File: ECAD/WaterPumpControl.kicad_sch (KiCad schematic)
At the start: 2 parts, among them Q7 NCE3018AS, Q8 NCE3018AS

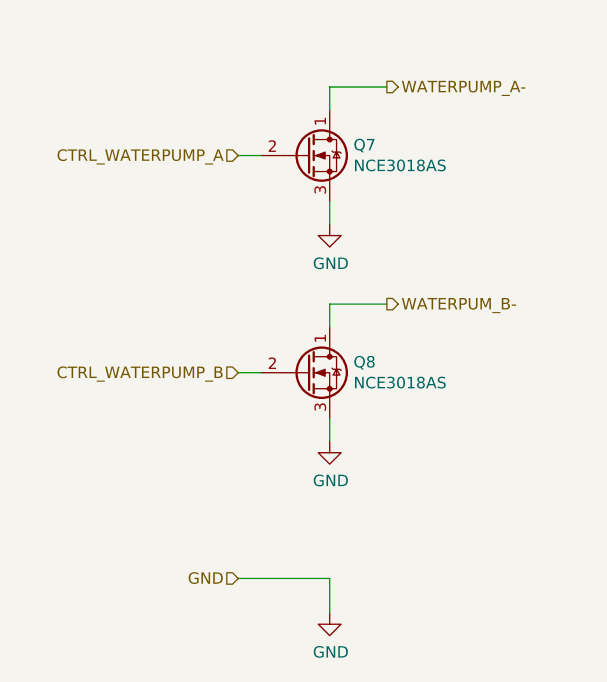
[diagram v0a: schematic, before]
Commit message: pcb layout has started, still ned to make 5V to 3.3V power supply, add dip switch do individually control input power of each switch, 5V or 12V
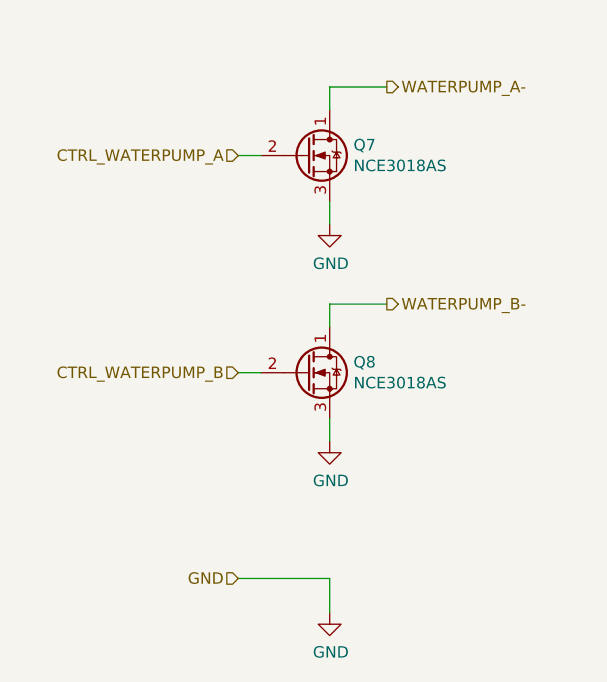
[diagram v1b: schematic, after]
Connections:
- net WATERPUM_B- renamed WATERPUMP_B-
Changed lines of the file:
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@@
     (effects (font (size 1.27 1.27)) (justify left))
   )
-  (hierarchical_label "WATERPUM_B-" (shape output) (at 158.75 100.33 0)
+  (hierarchical_label "WATERPUMP_B-" (shape output) (at 158.75 100.33 0)
     (effects (font (size 1.27 1.27)) (justify left))
   )

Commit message: finishing up pcb, only billonly bill of materials need to be done to be compatible with lc from jlcpcb
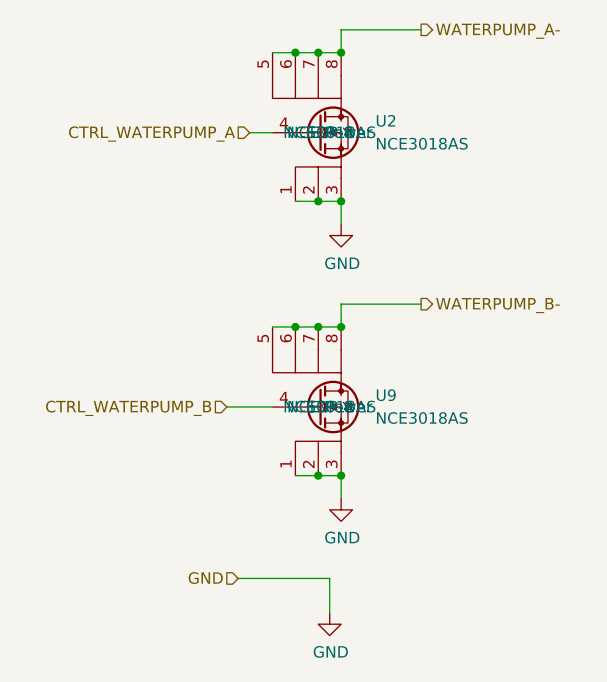
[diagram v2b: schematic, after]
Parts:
- removed Q7, Q8: NCE3018AS, Package_SO:SOP-8_3.9x4.9mm_P1.27mm, symbol Device:Q_NMOS_DGS
- added U2, U9: NCE3018AS, Package_SO:SO-8_3.9x4.9mm_P1.27mm, symbol Transistors:NCE3018AS
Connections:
- net CTRL_WATERPUMP_A: now also U2.4
- net CTRL_WATERPUMP_B: now also U9.4
- net GND: now also U2.1, U2.2, U2.3, U9.1, U9.2, U9.3
- net WATERPUMP_A-: now also U2.5, U2.6, U2.7, U2.8
- net WATERPUMP_B-: now also U9.5, U9.6, U9.7, U9.8
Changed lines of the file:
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@@
 (kicad_sch (version 20210126) (generator eeschema)
   (paper "A4")
-  (wire (pts (xy 142.24 83.82) (xy 144.78 83.82))
-    (stroke (width 0) (type solid) (color 0 0 0 0))
-  )
-  (wire (pts (xy 142.24 107.95) (xy 144.78 107.95))
+  (junction (at 148.59 72.39) (diameter 0.9144) (color 0 0 0 0))
+  (junction (at 148.59 102.87) (diameter 0.9144) (color 0 0 0 0))
+  (junction (at 151.13 72.39) (diameter 0.9144) (color 0 0 0 0))
+  (junction (at 151.13 88.9) (diameter 0.9144) (color 0 0 0 0))
+  (junction (at 151.13 102.87) (diameter 0.9144) (color 0 0 0 0))
+  (junction (at 151.13 119.38) (diameter 0.9144) (color 0 0 0 0))
+  (junction (at 153.67 72.39) (diameter 0.9144) (color 0 0 0 0))
+  (junction (at 153.67 88.9) (diameter 0.9144) (color 0 0 0 0))
+  (junction (at 153.67 102.87) (diameter 0.9144) (color 0 0 0 0))
+  (junction (at 153.67 119.38) (diameter 0.9144) (color 0 0 0 0))
+  (wire (pts (xy 140.97 111.76) (xy 146.05 111.76))
     (stroke (width 0) (type solid) (color 0 0 0 0))
   )
@@
     (stroke (width 0) (type solid) (color 0 0 0 0))
   )
-  (wire (pts (xy 152.4 76.2) (xy 158.75 76.2))
+  (wire (pts (xy 143.51 81.28) (xy 146.05 81.28))
     (stroke (width 0) (type solid) (color 0 0 0 0))
   )
-  (wire (pts (xy 152.4 78.74) (xy 152.4 76.2))
+  (wire (pts (xy 146.05 72.39) (xy 148.59 72.39))
     (stroke (width 0) (type solid) (color 0 0 0 0))
   )
-  (wire (pts (xy 152.4 88.9) (xy 152.4 91.44))
+  (wire (pts (xy 146.05 102.87) (xy 148.59 102.87))
     (stroke (width 0) (type solid) (color 0 0 0 0))
   )
-  (wire (pts (xy 152.4 100.33) (xy 158.75 100.33))
+  (wire (pts (xy 148.59 72.39) (xy 151.13 72.39))
     (stroke (width 0) (type solid) (color 0 0 0 0))
   )
-  (wire (pts (xy 152.4 102.87) (xy 152.4 100.33))
+  (wire (pts (xy 148.59 88.9) (xy 151.13 88.9))
     (stroke (width 0) (type solid) (color 0 0 0 0))
   )
-  (wire (pts (xy 152.4 113.03) (xy 152.4 115.57))
+  (wire (pts (xy 148.59 102.87) (xy 151.13 102.87))
+    (stroke (width 0) (type solid) (color 0 0 0 0))
+  )
+  (wire (pts (xy 148.59 119.38) (xy 151.13 119.38))
+    (stroke (width 0) (type solid) (color 0 0 0 0))
+  )
+  (wire (pts (xy 151.13 72.39) (xy 153.67 72.39))
+    (stroke (width 0) (type solid) (color 0 0 0 0))
+  )
+  (wire (pts (xy 151.13 88.9) (xy 153.67 88.9))
+    (stroke (width 0) (type solid) (color 0 0 0 0))
+  )
+  (wire (pts (xy 151.13 102.87) (xy 153.67 102.87))
+    (stroke (width 0) (type solid) (color 0 0 0 0))
+  )
+  (wire (pts (xy 151.13 119.38) (xy 153.67 119.38))
     (stroke (width 0) (type solid) (color 0 0 0 0))
   )
@@
     (stroke (width 0) (type solid) (color 0 0 0 0))
   )
-  (hierarchical_label "CTRL_WATERPUMP_A" (shape input) (at 142.24 83.82 180)
-    (effects (font (size 1.27 1.27)) (justify right))
+  (wire (pts (xy 153.67 69.85) (xy 162.56 69.85))
+    (stroke (width 0) (type solid) (color 0 0 0 0))
   )
-  (hierarchical_label "CTRL_WATERPUMP_B" (shape input) (at 142.24 107.95 180)
+  (wire (pts (xy 153.67 72.39) (xy 153.67 69.85))
+    (stroke (width 0) (type solid) (color 0 0 0 0))
+  )
+  (wire (pts (xy 153.67 88.9) (xy 153.67 91.44))
+    (stroke (width 0) (type solid) (color 0 0 0 0))
+  )
+  (wire (pts (xy 153.67 100.33) (xy 162.56 100.33))
+    (stroke (width 0) (type solid) (color 0 0 0 0))
+  )
+  (wire (pts (xy 153.67 102.87) (xy 153.67 100.33))
+    (stroke (width 0) (type solid) (color 0 0 0 0))
+  )
+  (wire (pts (xy 153.67 119.38) (xy 153.67 121.92))
+    (stroke (width 0) (type solid) (color 0 0 0 0))
+  )
+  (hierarchical_label "CTRL_WATERPUMP_B" (shape input) (at 140.97 111.76 180)
     (effects (font (size 1.27 1.27)) (justify right))
   )
@@
     (effects (font (size 1.27 1.27)) (justify right))
   )
-  (hierarchical_label "WATERPUMP_A-" (shape output) (at 158.75 76.2 0)
+  (hierarchical_label "CTRL_WATERPUMP_A" (shape input) (at 143.51 81.28 180)
+    (effects (font (size 1.27 1.27)) (justify right))
+  )
+  (hierarchical_label "WATERPUMP_A-" (shape output) (at 162.56 69.85 0)
     (effects (font (size 1.27 1.27)) (justify left))
   )
-  (hierarchical_label "WATERPUMP_B-" (shape output) (at 158.75 100.33 0)
+  (hierarchical_label "WATERPUMP_B-" (shape output) (at 162.56 100.33 0)
     (effects (font (size 1.27 1.27)) (justify left))
-  )
-  (symbol (lib_id "power:GND") (at 152.4 91.44 0) (unit 1)
-    (in_bom yes) (on_board yes)
-    (property "Reference" "#PWR0136" (id 0) (at 152.4 97.79 0)
-      (effects (font (size 1.27 1.27)) hide)
-    )
-    (property "Value" "GND" (id 1) (at 152.527 95.8342 0))
-    (property "Footprint" "" (id 2) (at 152.4 91.44 0)
-      (effects (font (size 1.27 1.27)) hide)
-    )
-    (property "Datasheet" "" (id 3) (at 152.4 91.44 0)
-      (effects (font (size 1.27 1.27)) hide)
-    )
-    (pin "1")
-  )
-  (symbol (lib_id "power:GND") (at 152.4 115.57 0) (unit 1)
-    (in_bom yes) (on_board yes)
-    (property "Reference" "#PWR0137" (id 0) (at 152.4 121.92 0)
-      (effects (font (size 1.27 1.27)) hide)
-    )
-    (property "Value" "GND" (id 1) (at 152.527 119.9642 0))
-    (property "Footprint" "" (id 2) (at 152.4 115.57 0)
-      (effects (font (size 1.27 1.27)) hide)
-    )
-    (property "Datasheet" "" (id 3) (at 152.4 115.57 0)
-      (effects (font (size 1.27 1.27)) hide)
-    )
-    (pin "1")
   )
   (symbol (lib_id "power:GND") (at 152.4 134.62 0) (unit 1)
@@
     (pin "1")
   )
-  (symbol (lib_id "Device:Q_NMOS_DGS") (at 149.86 83.82 0) (unit 1)
+  (symbol (lib_id "power:GND") (at 153.67 91.44 0) (unit 1)
     (in_bom yes) (on_board yes)
-    (property "Reference" "Q7" (id 0) (at 155.0416 82.6516 0)
-      (effects (font (size 1.27 1.27)) (justify left))
-    )
-    (property "Value" "NCE3018AS" (id 1) (at 155.0416 84.963 0)
-      (effects (font (size 1.27 1.27)) (justify left))
-    )
-    (property "Footprint" "Package_SO:SOP-8_3.9x4.9mm_P1.27mm" (id 2) (at 154.94 81.28 0)
+    (property "Reference" "#PWR0136" (id 0) (at 153.67 97.79 0)
       (effects (font (size 1.27 1.27)) hide)
     )
-    (property "Datasheet" "~" (id 3) (at 149.86 83.82 0)
+    (property "Value" "GND" (id 1) (at 153.797 95.8342 0))
+    (property "Footprint" "" (id 2) (at 153.67 91.44 0)
+      (effects (font (size 1.27 1.27)) hide)
+    )
+    (property "Datasheet" "" (id 3) (at 153.67 91.44 0)
       (effects (font (size 1.27 1.27)) hide)
     )
     (pin "1")
-    (pin "2")
-    (pin "3")
   )
-  (symbol (lib_id "Device:Q_NMOS_DGS") (at 149.86 107.95 0) (unit 1)
+  (symbol (lib_id "power:GND") (at 153.67 121.92 0) (unit 1)
     (in_bom yes) (on_board yes)
-    (property "Reference" "Q8" (id 0) (at 155.0416 106.7816 0)
-      (effects (font (size 1.27 1.27)) (justify left))
-    )
-    (property "Value" "NCE3018AS" (id 1) (at 155.0416 109.093 0)
-      (effects (font (size 1.27 1.27)) (justify left))
-    )
-    (property "Footprint" "Package_SO:SOP-8_3.9x4.9mm_P1.27mm" (id 2) (at 154.94 105.41 0)
+    (property "Reference" "#PWR0101" (id 0) (at 153.67 128.27 0)
       (effects (font (size 1.27 1.27)) hide)
     )
-    (property "Datasheet" "~" (id 3) (at 149.86 107.95 0)
+    (property "Value" "GND" (id 1) (at 153.797 126.3142 0))
+    (property "Footprint" "" (id 2) (at 153.67 121.92 0)
+      (effects (font (size 1.27 1.27)) hide)
+    )
+    (property "Datasheet" "" (id 3) (at 153.67 121.92 0)
       (effects (font (size 1.27 1.27)) hide)
     )
     (pin "1")
+  )
+  (symbol (lib_name "Transistors:NCE3018AS_1") (lib_id "Transistors:NCE3018AS") (at 152.4 81.28 0) (unit 1)
+    (in_bom yes) (on_board yes)
+    (property "Reference" "U2" (id 0) (at 157.48 80.01 0)
+      (effects (font (size 1.27 1.27)) (justify left))
+    )
+    (property "Value" "NCE3018AS" (id 1) (at 157.48 82.55 0)
+      (effects (font (size 1.27 1.27)) (justify left))
+    )
+    (property "Footprint" "Package_SO:SO-8_3.9x4.9mm_P1.27mm" (id 2) (at 153.67 67.31 0)
+      (effects (font (size 1.27 1.27)) hide)
+    )
+    (property "Datasheet" "https://datasheetspdf.com/pdf-file/1273153/NCEPowerSemiconductor/NCE3018AS/1" (id 3) (at 153.67 67.31 0)
+      (effects (font (size 1.27 1.27)) hide)
+    )
+    (property "Manufacturer Number" "NCE3018AS" (id 4) (at 152.4 81.28 0))
+    (property "Package" "SOP-8" (id 5) (at 152.4 81.28 0))
+    (property "Manufacturer" "NCE Power" (id 6) (at 152.4 81.28 0))
+    (pin "5")
+    (pin "4")
+    (pin "1")
     (pin "2")
     (pin "3")
+    (pin "6")
+    (pin "7")
+    (pin "8")
+  )
+  (symbol (lib_id "Transistors:NCE3018AS") (at 152.4 111.76 0) (unit 1)
+    (in_bom yes) (on_board yes)
+    (property "Reference" "U9" (id 0) (at 157.48 110.49 0)
+      (effects (font (size 1.27 1.27)) (justify left))
+    )
+    (property "Value" "NCE3018AS" (id 1) (at 157.48 113.03 0)
+      (effects (font (size 1.27 1.27)) (justify left))
+    )
+    (property "Footprint" "Package_SO:SO-8_3.9x4.9mm_P1.27mm" (id 2) (at 153.67 97.79 0)
+      (effects (font (size 1.27 1.27)) hide)
+    )
+    (property "Datasheet" "https://datasheetspdf.com/pdf-file/1273153/NCEPowerSemiconductor/NCE3018AS/1" (id 3) (at 153.67 97.79 0)
+      (effects (font (size 1.27 1.27)) hide)
+    )
+    (property "Manufacturer Number" "NCE3018AS" (id 4) (at 152.4 111.76 0))
+    (property "Package" "SOP-8" (id 5) (at 152.4 111.76 0))
+    (property "Manufacturer" "NCE Power" (id 6) (at 152.4 111.76 0))
+    (pin "5")
+    (pin "4")
+    (pin "1")
+    (pin "2")
+    (pin "3")
+    (pin "6")
+    (pin "7")
+    (pin "8")
   )
 )

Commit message: adding production and step files
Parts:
- U2, U9: Package SOP-8 -> SOP-8_150mil
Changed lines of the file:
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@@
     )
     (property "Manufacturer Number" "NCE3018AS" (id 4) (at 152.4 81.28 0))
-    (property "Package" "SOP-8" (id 5) (at 152.4 81.28 0))
+    (property "Package" "SOP-8_150mil" (id 5) (at 152.4 81.28 0))
     (property "Manufacturer" "NCE Power" (id 6) (at 152.4 81.28 0))
     (pin "5")
@@
     )
     (property "Manufacturer Number" "NCE3018AS" (id 4) (at 152.4 111.76 0))
-    (property "Package" "SOP-8" (id 5) (at 152.4 111.76 0))
+    (property "Package" "SOP-8_150mil" (id 5) (at 152.4 111.76 0))
     (property "Manufacturer" "NCE Power" (id 6) (at 152.4 111.76 0))
     (pin "5")
